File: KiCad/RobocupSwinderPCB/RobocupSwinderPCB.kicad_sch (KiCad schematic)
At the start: 27 parts, among them J1 Barrel_Jack, M1 Stepper_Motor_bipolar, M2 Stepper_Motor_bipolar, SW1 Limit_Switch, SW2 Limit_Switch, SW3 SW_SPST, U1 Teensy4.1, U3 LM7805_TO220

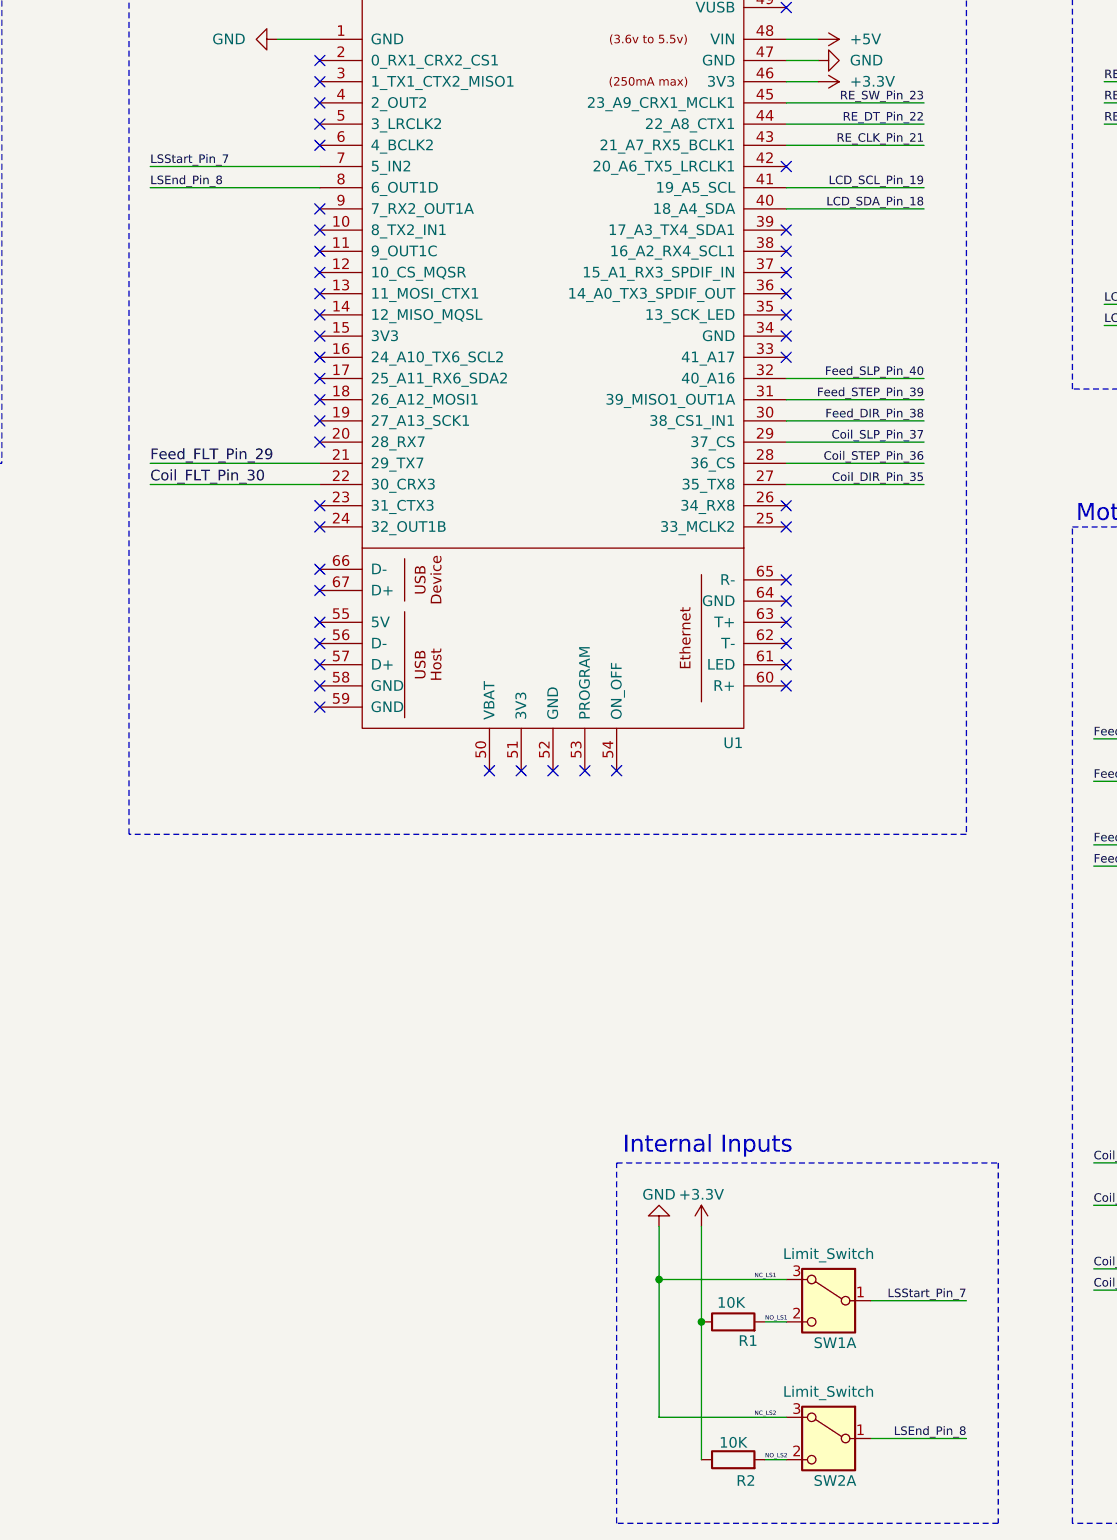
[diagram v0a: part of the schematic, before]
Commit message: Fixed various errors, add two pause states to let user fix wire positions and a back feed on zero to prevent misaligned zero.
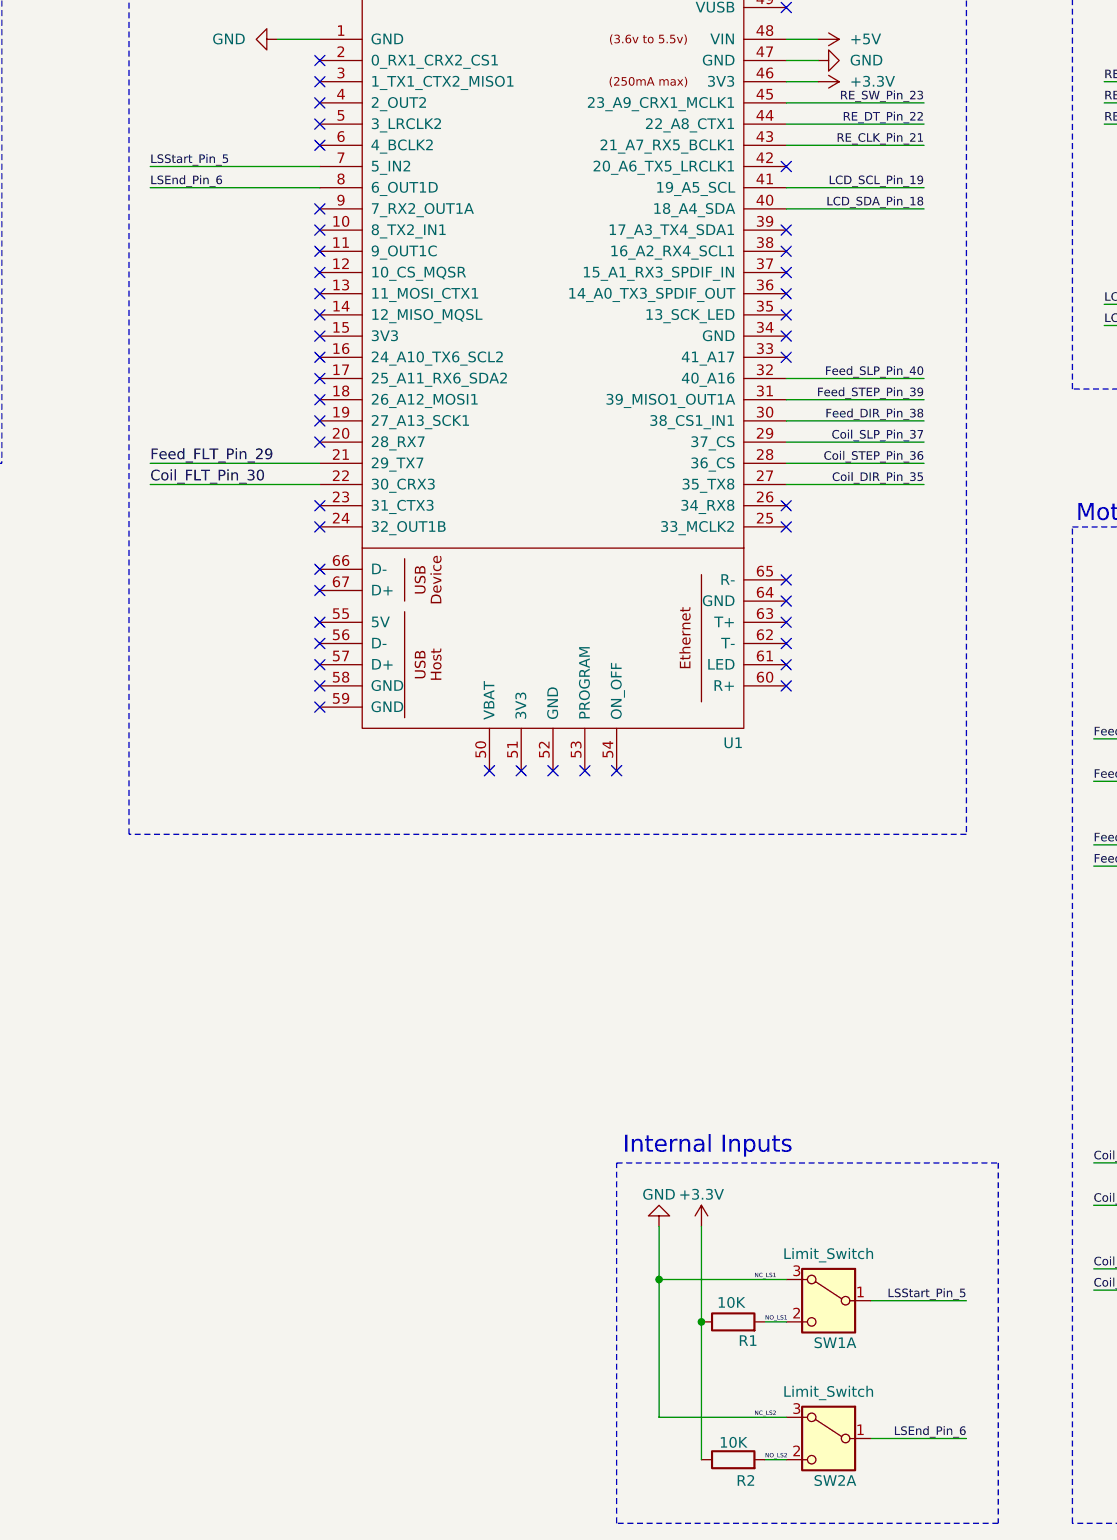
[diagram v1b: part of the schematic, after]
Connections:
- net LSEnd_Pin_8 renamed LSEnd_Pin_6
- net LSStart_Pin_7 renamed LSStart_Pin_5
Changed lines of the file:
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@@
 		)
 	)
-	(label "LSStart_Pin_7"
+	(label "LSStart_Pin_5"
 		(at 163.83 63.5 0)
 		(effects
@@
 		)
 	)
-	(label "LSStart_Pin_7"
+	(label "LSStart_Pin_5"
 		(at 261.62 199.39 180)
 		(effects
@@
 		)
 	)
-	(label "LSEnd_Pin_8"
+	(label "LSEnd_Pin_6"
 		(at 261.62 215.9 180)
 		(effects
@@
 		)
 	)
-	(label "LSEnd_Pin_8"
+	(label "LSEnd_Pin_6"
 		(at 163.83 66.04 0)
 		(effects
